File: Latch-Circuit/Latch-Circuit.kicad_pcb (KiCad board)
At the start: 2 copper layers, 90 x 50 mm, 82 parts, among them J1 BM02B-PASS-1-TF, J10 BM02B-PASS-1-TF, J2 BM03B-PASS-1-TF, J3 BM02B-PASS-1-TF, J4 BM02B-PASS-1-TF, J5 BM02B-PASS-1-TF, J6 BM02B-PASS-1-TF, J7 B2P-VH, J8 BM02B-PASS-1-TF, J9 BM02B-PASS-1-TF, K1 G5Q-1A4_DC12, K2 G5Q-1A4_DC12, K3 G5Q-1A4_DC12, Q1 DMP3098LQ-7, Q10 2N7002K-AU, Q11 2N7002K-AU, Q12 PJA3439-AU_R1_000A1, Q13 PJA3439-AU_R1_000A1, Q2 2N7002K-AU, Q3 PJA3439-AU_R1_000A1, Q4 2N7002K-AU, Q5 PJA3439-AU_R1_000A1, Q6 2N7002K-AU, Q7 2N7002K-AU, Q8 PJA3439-AU_R1_000A1, Q9 PJA3439-AU_R1_000A1

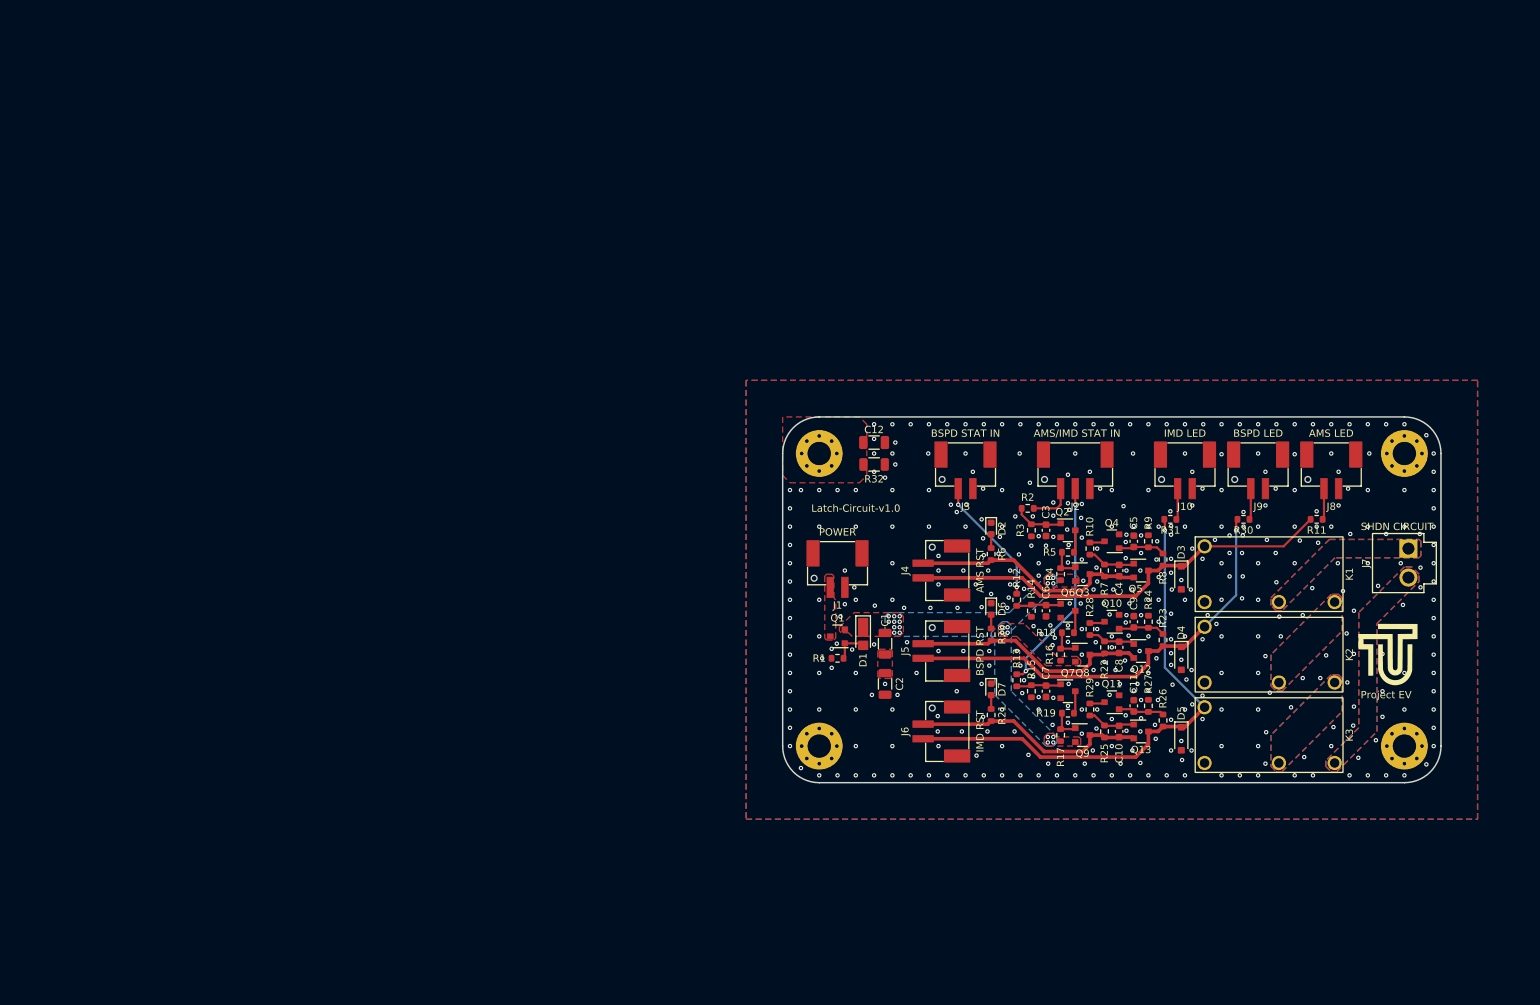
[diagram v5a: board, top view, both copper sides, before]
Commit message: 原点位置の修正
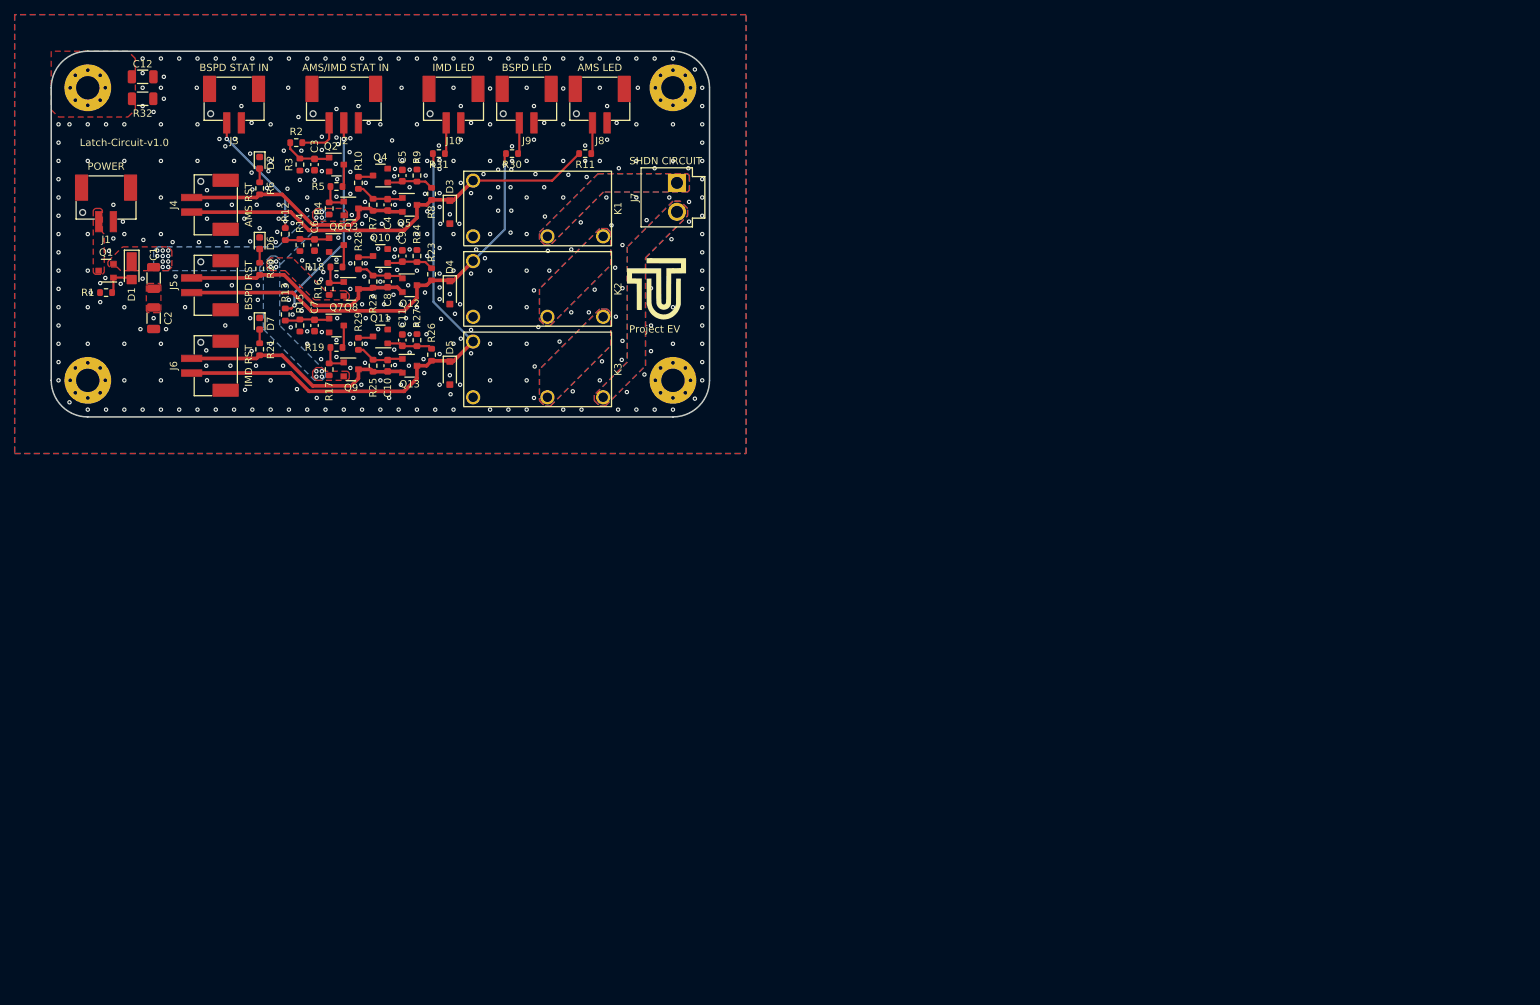
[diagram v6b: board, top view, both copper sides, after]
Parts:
- moved J7 111.8 mm to (85.5, 18.0)
- moved C1 111.8 mm to (14.0, 31.0)
- moved C10 111.8 mm to (46.0, 43.0)
- moved C11 111.8 mm to (48.0, 39.5)
- moved C12 111.8 mm to (12.5, 3.50)
- moved C2 111.8 mm to (14.0, 36.5)
- moved C3 111.8 mm to (36.0, 15.5)
- moved C4 111.8 mm to (46.0, 21.0)
- moved C5 111.8 mm to (48.0, 17.0)
- moved C6 111.8 mm to (36.0, 26.5)
- moved C7 111.8 mm to (36.0, 37.5)
- moved C8 111.8 mm to (46.0, 31.5)
- moved C9 111.8 mm to (48.0, 28.0)
- moved D1 111.8 mm to (11.0, 30.0)
- moved D2 111.8 mm to (28.5, 15.2)
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
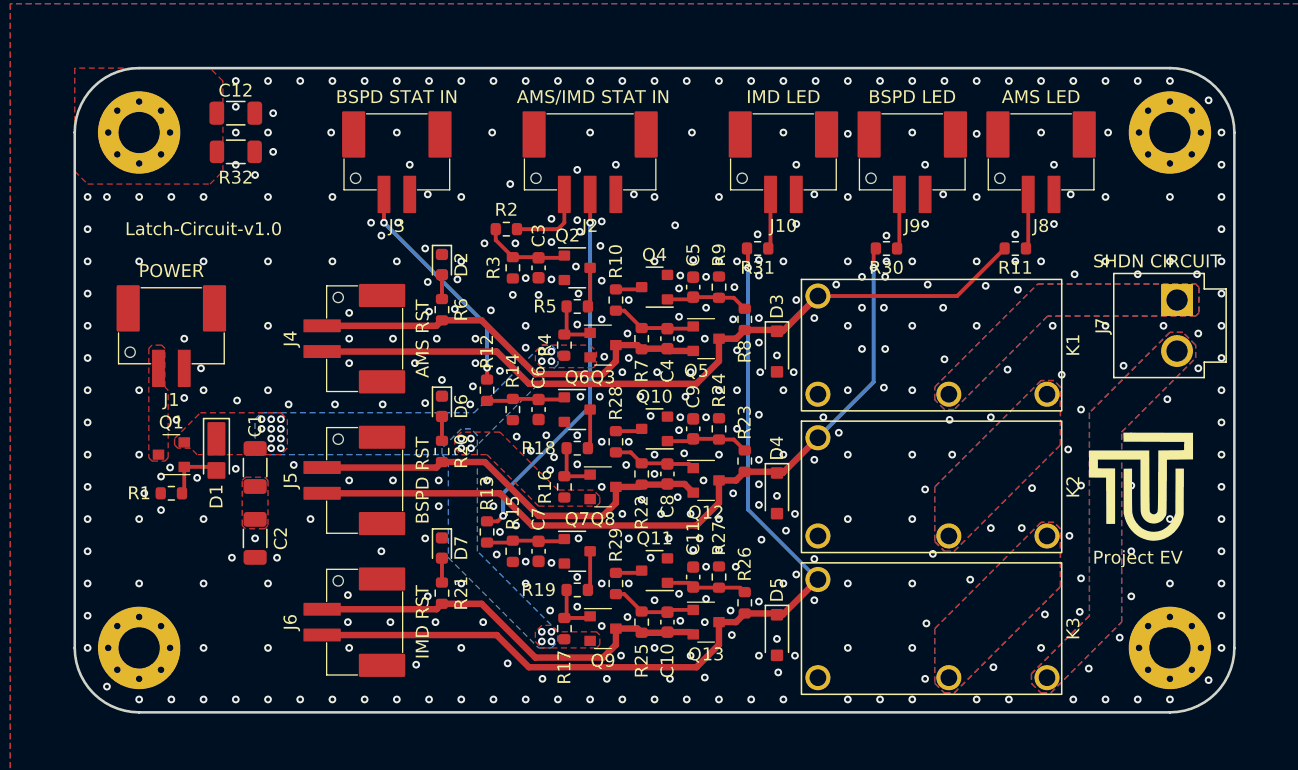
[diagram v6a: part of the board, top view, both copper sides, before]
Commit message: シャットダウンチェック用のTP追加
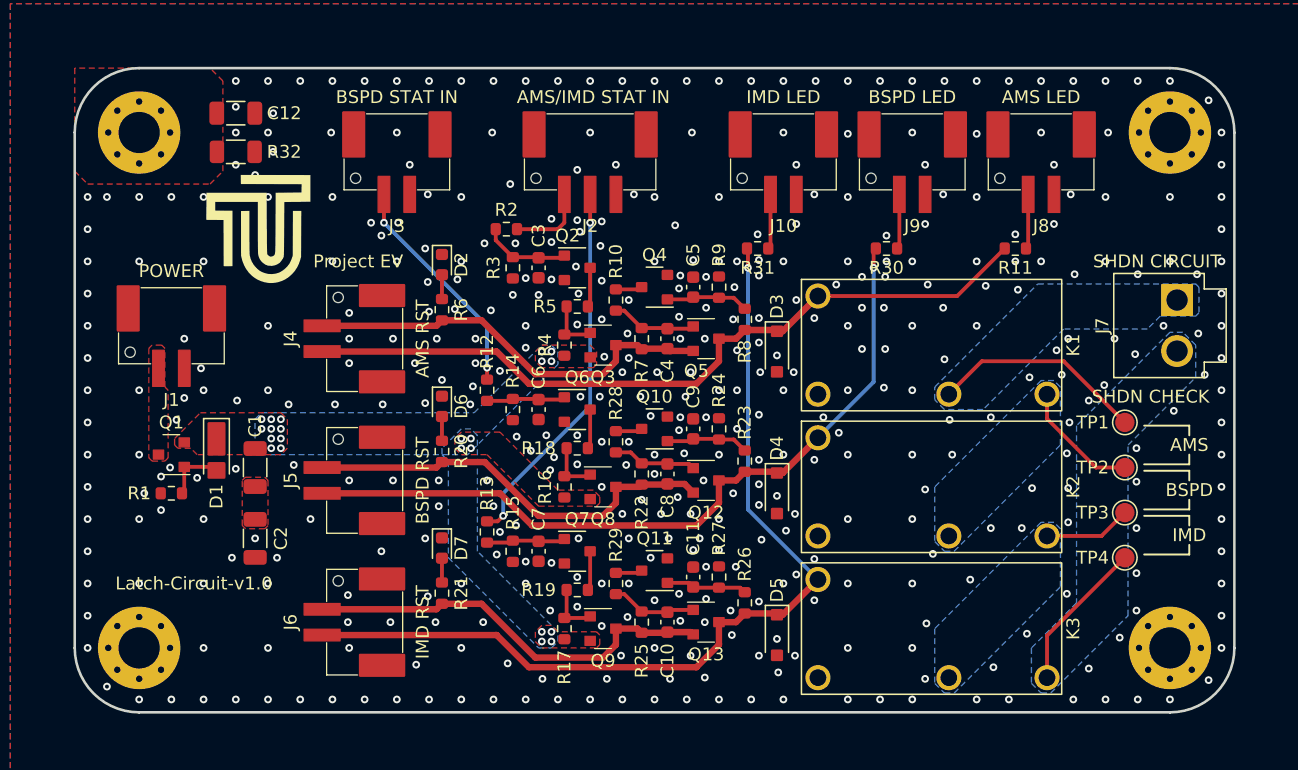
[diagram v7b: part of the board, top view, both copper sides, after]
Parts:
- added TP1: TestPoint, TestPoint:TestPoint_Pad_D1.5mm, F.Cu at (81.5, 27.5)
- added TP2: TestPoint, TestPoint:TestPoint_Pad_D1.5mm, F.Cu at (81.5, 31.0)
- added TP3: TestPoint, TestPoint:TestPoint_Pad_D1.5mm, F.Cu at (81.5, 34.5)
- added TP4: TestPoint, TestPoint:TestPoint_Pad_D1.5mm, F.Cu at (81.5, 38.0)
- moved G*** 71.4 mm to (14.0, 12.5)
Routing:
- net /SHDN_IN: track 0.00 -> 16.7 mm
- net /SHDN_OUT: track 0.00 -> 11.8 mm
- net Net-(K1-Pad3): track 0.00 -> 9.51 mm
- net Net-(K2-Pad3): track 0.00 -> 6.79 mm
- net GND: vias 440 -> 439
- removed copper zone on F.Cu, net /SHDN_IN
- removed copper zone on F.Cu, net /SHDN_OUT
- removed copper zone on F.Cu, net Net-(K1-Pad3)
- removed copper zone on F.Cu, net Net-(K2-Pad3)
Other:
- board text added: "AMS"
- board text added: "BSPD"
- board text added: "IMD"
- board text added: "SHDN CHECK"

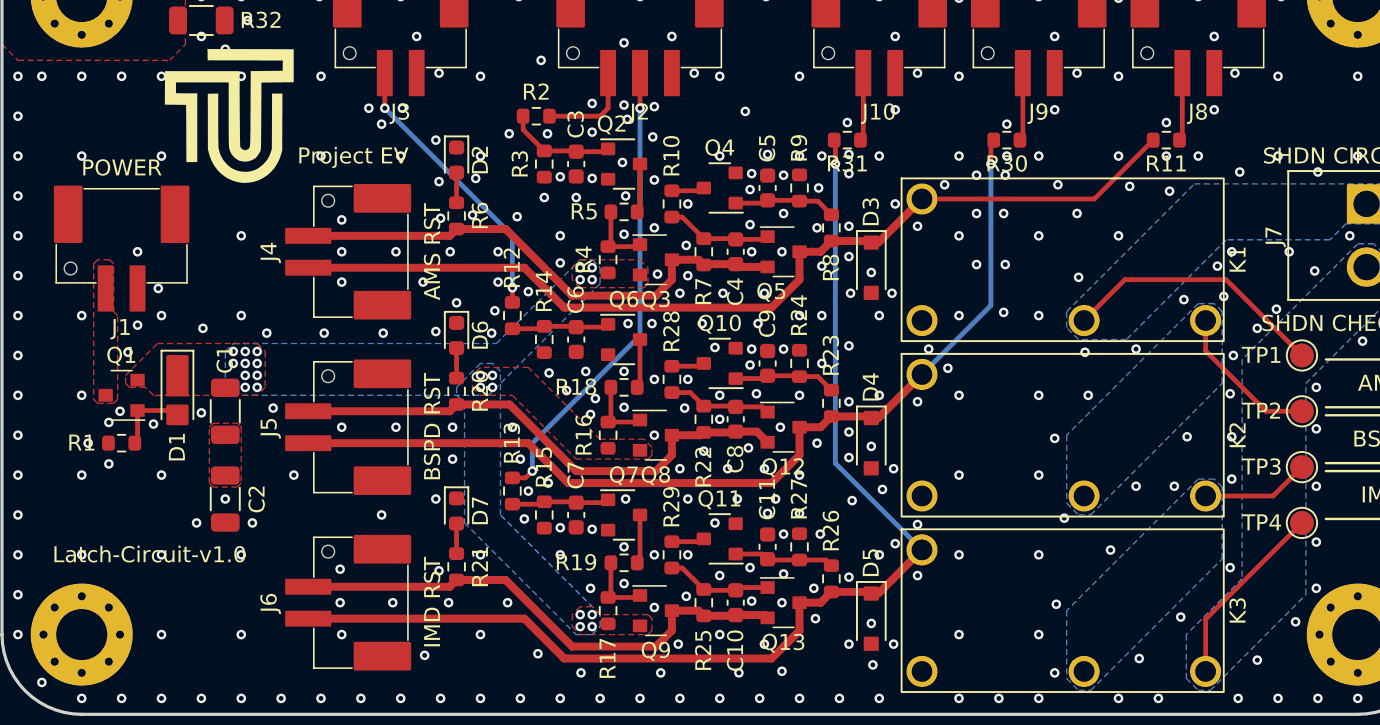
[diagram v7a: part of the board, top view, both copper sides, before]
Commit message: 1ピン識別子追加
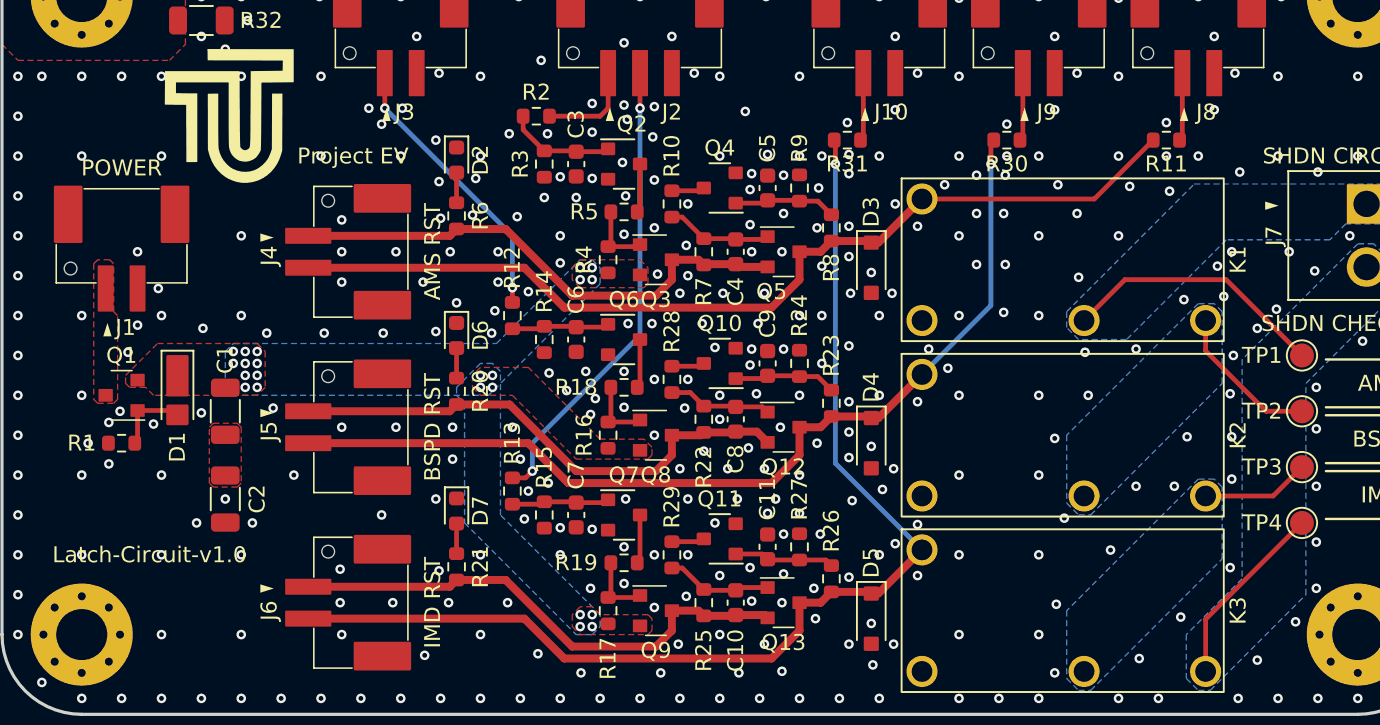
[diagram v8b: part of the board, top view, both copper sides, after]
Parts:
- added REF**: Identifier_1pin, ProjectEV:Identifier_1pin, F.Cu at (24.0, 12.0)
- added REF**: Identifier_1pin, ProjectEV:Identifier_1pin, F.Cu at (17.0, 42.0)
- added REF**: Identifier_1pin, ProjectEV:Identifier_1pin, F.Cu at (38.0, 12.0)
- added REF**: Identifier_1pin, ProjectEV:Identifier_1pin, F.Cu at (80.0, 18.0)
- added REF**: Identifier_1pin, ProjectEV:Identifier_1pin, F.Cu at (17.0, 31.0)
- added REF**: Identifier_1pin, ProjectEV:Identifier_1pin, F.Cu at (74.0, 12.0)
- added REF**: Identifier_1pin, ProjectEV:Identifier_1pin, F.Cu at (17.0, 20.0)
- added REF**: Identifier_1pin, ProjectEV:Identifier_1pin, F.Cu at (54.0, 12.0)
- added REF**: Identifier_1pin, ProjectEV:Identifier_1pin, F.Cu at (64.0, 12.0)
- added REF**: Identifier_1pin, ProjectEV:Identifier_1pin, F.Cu at (6.50, 25.5)
